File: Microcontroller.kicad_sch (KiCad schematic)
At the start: 17 parts, among them IC3 W25Q128JVSIQ, IC4 ESP32-S3R8, Q1 40MHz

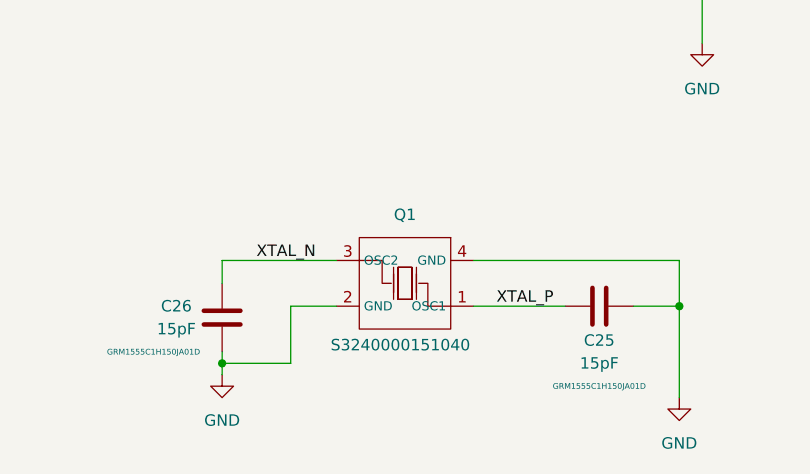
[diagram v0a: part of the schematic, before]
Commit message: Some small fixes
Swapped the pins on the oscillator
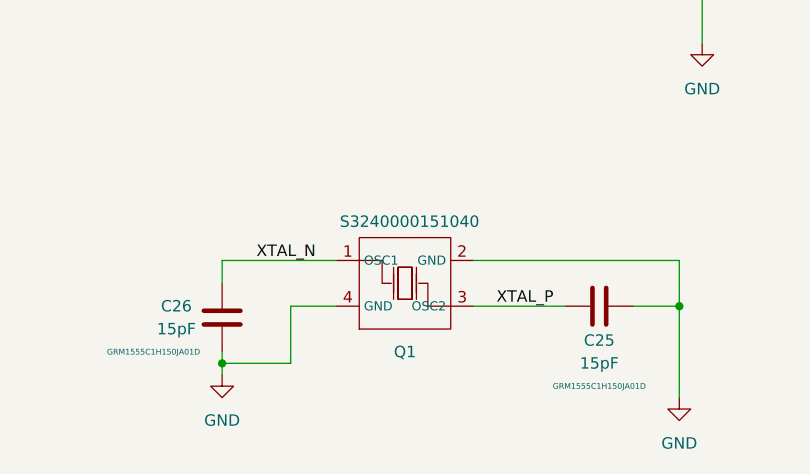
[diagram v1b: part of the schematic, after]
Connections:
- net XTAL_N: now also Q1.1 (OSC1); no longer Q1.3 (OSC2)
- net XTAL_P: now also Q1.3 (OSC2); no longer Q1.1 (OSC1)
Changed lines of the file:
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@@
 		(lib_id "S3240000151040:S3240000151040")
 		(at 234.95 144.78 0)
-		(mirror y)
+		(mirror x)
 		(unit 1)
 		(exclude_from_sim no)
@@
 		(dnp no)
 		(property "Reference" "Q1"
-			(at 234.95 137.16 0)
+			(at 234.95 152.4 0)
 			(effects
 				(font
@@
 		)
 		(property "Value" "40MHz"
-			(at 235.458 141.224 0)
+			(at 234.442 148.336 0)
 			(effects
 				(font
@@
 		)
 		(property "Footprint" "S3240000151040:CRYSTAL-SMD_4P-L3.2-W2.5-BL"
-			(at 235.458 140.97 0)
+			(at 234.442 148.59 0)
 			(effects
 				(font
@@
 		)
 		(property "Datasheet" "https://atta.szlcsc.com/upload/public/pdf/source/20191012/C431172_99BCDFC5E39E114929AE7F9C9DED2B9F.pdf"
-			(at 235.458 140.716 0)
+			(at 234.442 148.844 0)
 			(effects
 				(font
@@
 		)
 		(property "Description" "Crystal Type:贴片晶振 Frequency: Normal temperature Frequency Tolerance:±10ppm Normal temperature Frequency Tolerance:±10ppm External load capacitor: Equivalent Series Resistance (ESR):40Ω Operating Temperature: Operating Temperature:"
-			(at 235.204 141.478 0)
+			(at 234.696 148.082 0)
 			(effects
 				(font
@@
 		)
 		(property "Manufacturer Part" "S3240000151040"
-			(at 235.458 141.224 0)
+			(at 234.442 148.336 0)
 			(effects
 				(font
@@
 		)
 		(property "Manufacturer" "JGHC(晶光华)"
-			(at 234.95 140.97 0)
+			(at 234.95 148.59 0)
 			(effects
 				(font
@@
 		)
 		(property "Supplier Part" "C426990"
-			(at 235.458 141.224 0)
+			(at 234.442 148.336 0)
 			(effects
 				(font
@@
 		)
 		(property "Supplier" "LCSC"
-			(at 235.204 141.224 0)
+			(at 234.696 148.336 0)
 			(effects
 				(font
@@
 		)
 		(property "LCSC Part Name" "40MHz ±10ppm 15pF"
-			(at 235.458 141.224 0)
+			(at 234.442 148.336 0)
 			(effects
 				(font
@@
 		)
 		(property "Footpirnt Name" "S3240000151040"
-			(at 234.442 151.638 0)
+			(at 235.458 137.922 0)
 			(effects
 				(font

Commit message: Changes to final schematic
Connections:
- net ESP_USB_DM renamed ESP_USB_D-
- net ESP_USB_DP renamed ESP_USB_D+
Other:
- note removed: "DA SLOJA LED ZA 3.3V DA SE ZNAE CHE RABOTI MOJE I ZA 12V KUM 3.3"
- moved on the sheet: C26
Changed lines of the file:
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@@
 	(generator_version "9.0")
 	(paper "A4")
-	(text "DA SLOJA LED ZA 3.3V DA SE ZNAE CHE RABOTI MOJE I ZA 12V KUM 3.3"
-		(exclude_from_sim no)
-		(at 224.79 24.13 0)
-		(effects
-			(font
-				(size 2 2)
-			)
-		)
-	)
 	(text "One capacitor close to each pin"
 		(exclude_from_sim no)
@@
 	)
 	(junction
-		(at 177.8 72.39)
+		(at 214.63 152.4)
 		(diameter 0)
 		(color 0 0 0 0)
 	)
 	(junction
-		(at 267.97 82.55)
+		(at 177.8 72.39)
 		(diameter 0)
 		(color 0 0 0 0)
 	)
 	(junction
-		(at 68.58 29.21)
+		(at 267.97 82.55)
 		(diameter 0)
 		(color 0 0 0 0)
 	)
 	(junction
-		(at 17.78 44.45)
+		(at 68.58 29.21)
 		(diameter 0)
 		(color 0 0 0 0)
 	)
 	(junction
-		(at 214.63 153.67)
+		(at 17.78 44.45)
 		(diameter 0)
 		(color 0 0 0 0)
@@
 	(wire
 		(pts
-			(xy 222.25 147.32) (xy 222.25 153.67)
+			(xy 222.25 147.32) (xy 222.25 152.4)
 		)
 		(stroke
@@
 	(wire
 		(pts
-			(xy 214.63 142.24) (xy 214.63 144.78)
+			(xy 214.63 142.24) (xy 214.63 143.51)
 		)
 		(stroke
@@
 	(wire
 		(pts
-			(xy 222.25 153.67) (xy 214.63 153.67)
-		)
-		(stroke
-			(width 0)
-			(type default)
-		)
-	)
-	(wire
-		(pts
-			(xy 214.63 153.67) (xy 214.63 154.94)
+			(xy 222.25 152.4) (xy 214.63 152.4)
 		)
 		(stroke
@@
 	(wire
 		(pts
+			(xy 214.63 152.4) (xy 214.63 154.94)
+		)
+		(stroke
+			(width 0)
+			(type default)
+		)
+	)
+	(wire
+		(pts
 			(xy 30.48 40.64) (xy 30.48 44.45)
 		)
@@
 	(wire
 		(pts
-			(xy 214.63 152.4) (xy 214.63 153.67)
+			(xy 214.63 151.13) (xy 214.63 152.4)
 		)
 		(stroke
@@
 		)
 	)
-	(label "ESP_USB_DM"
+	(label "ESP_USB_D-"
 		(at 134.62 114.3 0)
 		(effects
@@
 		)
 	)
-	(label "ESP_USB_DP"
+	(label "ESP_USB_D+"
 		(at 134.62 116.84 0)
 		(effects
@@
 		)
 	)
-	(global_label "ESP_USB_DM"
+	(global_label "ESP_USB_D-"
 		(shape input)
 		(at 153.67 114.3 0)
@@
 		)
 		(property "Intersheetrefs" "${INTERSHEET_REFS}"
-			(at 168.7503 114.3 0)
+			(at 168.8713 114.3 0)
 			(effects
 				(font
@@
 		)
 	)
-	(global_label "ESP_USB_DP"
+	(global_label "ESP_USB_D+"
 		(shape input)
 		(at 153.67 116.84 0)
@@
 		)
 		(property "Intersheetrefs" "${INTERSHEET_REFS}"
-			(at 168.5689 116.84 0)
+			(at 168.8713 116.84 0)
 			(effects
 				(font
@@
 	(symbol
 		(lib_id "Project Capacitors:GRM1555C1H150JA01D")
-		(at 214.63 148.59 0)
+		(at 214.63 147.32 0)
 		(mirror y)
 		(unit 1)
@@
 		(dnp no)
 		(property "Reference" "C26"
-			(at 209.55 147.32 0)
+			(at 209.55 146.05 0)
 			(effects
 				(font
@@
 		)
 		(property "Value" "15pF"
-			(at 209.55 149.86 0)
+			(at 209.55 148.59 0)
 			(effects
 				(font
@@
 		)
 		(property "Footprint" "GRM1555C1H150JA01D:CAPC1005X55N"
-			(at 213.6648 152.4 0)
+			(at 213.6648 151.13 0)
 			(effects
 				(font
@@
 		)
 		(property "Datasheet" "~"
-			(at 214.63 148.59 0)
+			(at 214.63 147.32 0)
 			(effects
 				(font
@@
 		)
 		(property "Description" "Unpolarized capacitor"
-			(at 214.63 148.59 0)
+			(at 214.63 147.32 0)
 			(effects
 				(font
@@
 		)
 		(property "Footprint Name" "GRM1555C1H150JA01D"
-			(at 207.01 152.4 0)
+			(at 207.01 151.13 0)
 			(effects
 				(font

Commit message: Minor changes to styling
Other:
- note added: "Microcontroller"
- note added: "Quartz"
- note added: "SPI Flash"
- moved on the sheet: C24, C25, C26, IC3, Q1
